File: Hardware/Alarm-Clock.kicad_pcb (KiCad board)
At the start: 2 copper layers, 100 x 61.6 mm, 26 parts, among them IC1 MEGA8-AI, Q1 16Mhz, X1 MINI-USB-32005-201

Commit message: update schematic and board
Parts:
- removed JP11: PINHD-1X4, Alarm-Clock:1X04
- Q1: moved to B.Cu
- turned Q1 to 270 degrees
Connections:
- net Net-(IC1-Pad2) renamed /PD4
- net Net-(IC1-Pad23) renamed /PC0
- net Net-(IC1-Pad24) renamed /PC1
- net Net-(IC1-Pad25) renamed /PC2
- net Net-(IC1-Pad26) renamed /PC3
- net Net-(IC1-Pad27) renamed /PC4
- net Net-(IC1-Pad28) renamed /PC5
- net Net-(IC1-Pad30) renamed /PD0
- net Net-(IC1-Pad31) renamed /PD1
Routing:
- net Net-(JP2-Pad5): track 116.4 -> 123.1 mm, vias 3 -> 2
- net N$59: track 6.67 -> 0.00 mm
- net Net-(C1-Pad2): track 328.2 -> 334.3 mm, vias 12 -> 4
- net N$58: track 6.11 -> 0.00 mm
- net Net-(DIS1-Pad4): track 35.7 -> 34.2 mm, vias 3 -> 2
- net Net-(R2-Pad2): vias 2 -> 0
- net Net-(R1-Pad2): vias 2 -> 0
- net Net-(JP2-Pad4): vias 3 -> 2
- net Net-(JP1-Pad7): vias 1 -> 0
- net Net-(IC1-Pad1): vias 1 -> 0
- net Net-(DIS1-Pad6): vias 3 -> 2
- net Net-(DIS1-Pad3): vias 1 -> 0
- net Net-(DIS1-Pad15): vias 2 -> 0
- net Net-(DIS1-Pad14): vias 1 -> 0
- net Net-(DIS1-Pad13): vias 1 -> 0
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
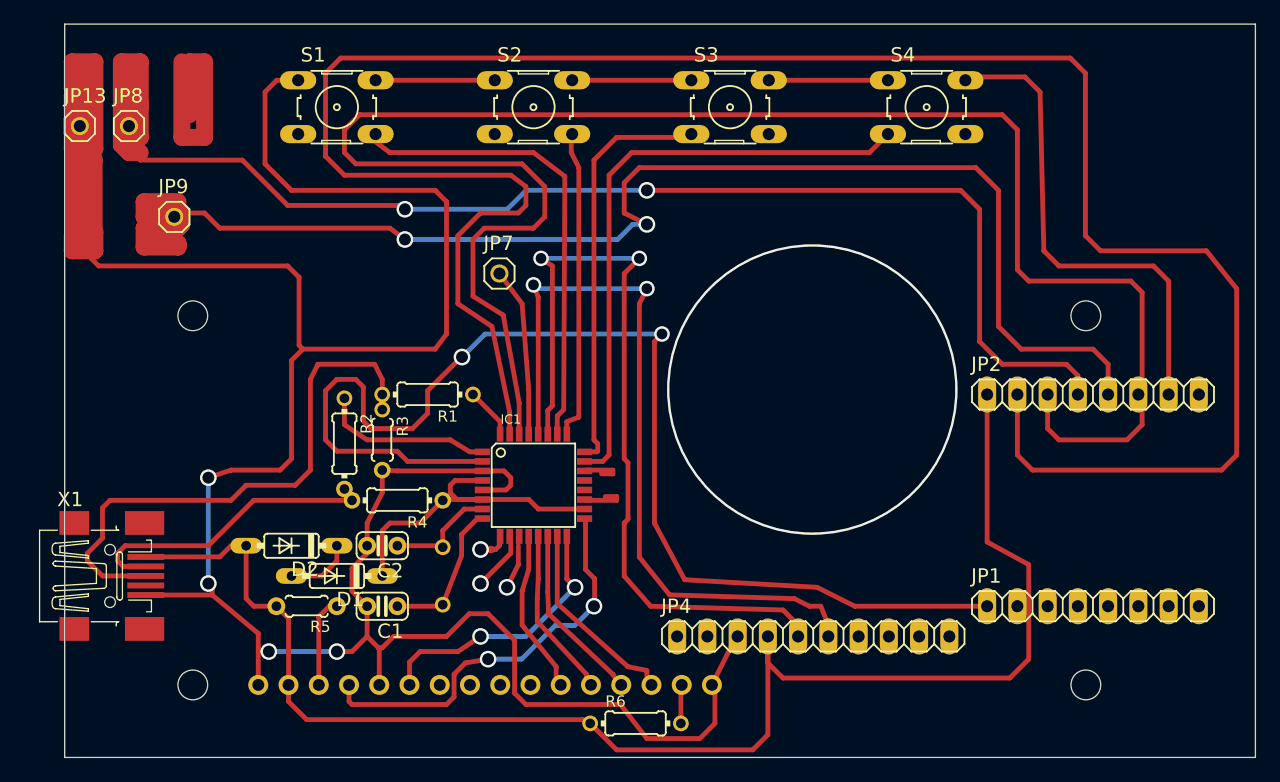
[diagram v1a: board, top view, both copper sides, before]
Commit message: Added 3d models to board
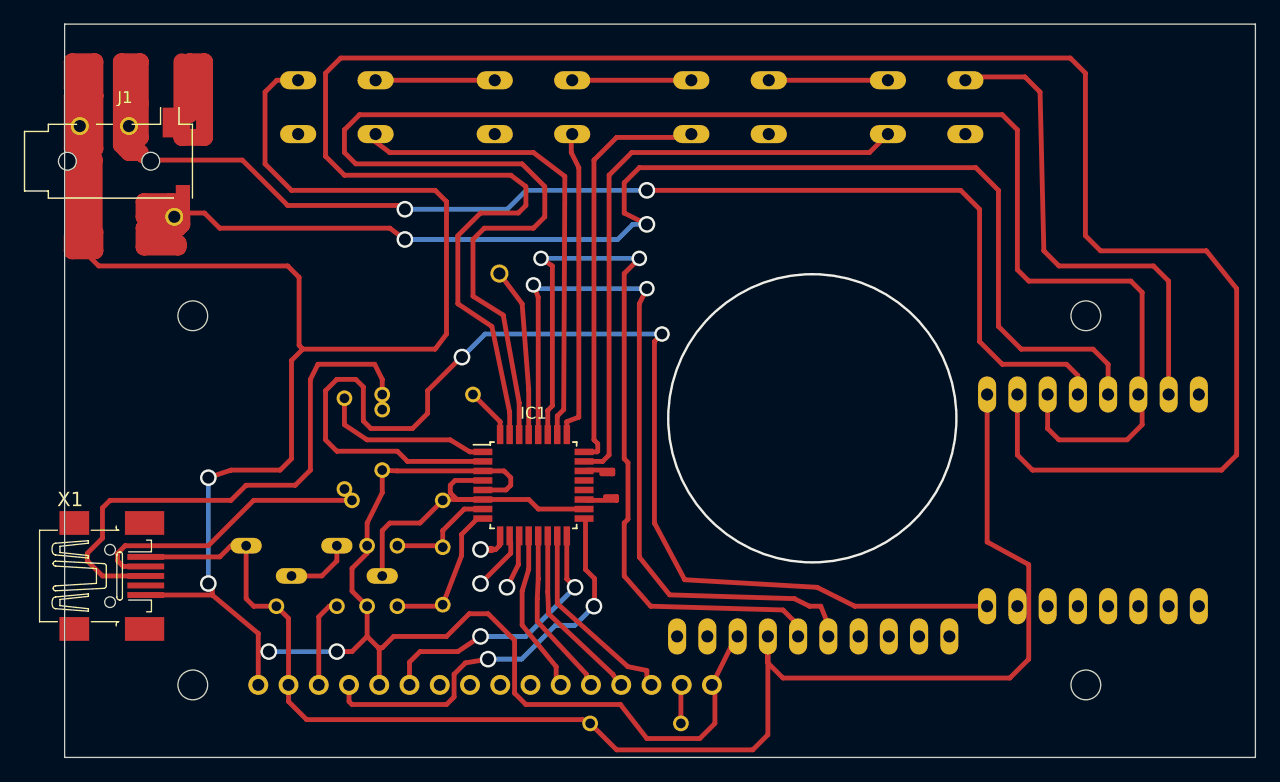
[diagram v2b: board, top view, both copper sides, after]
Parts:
- added J1: AudioJack3, Alarm-Clock:Jack_3.5mm_PJ320D_Horizontal, F.Cu at (103.5, 85.7)
- C1, C2, JP1, JP2, R1, R2, R3, R4, R5, R6, S1, S2, S3, S4: moved to B.Cu
- D1, D2: value 1N4148DO35-7 -> 1N4148; moved to B.Cu
- IC1: footprint Alarm-Clock:TQFP32-08 -> Package_QFP:TQFP-32_7x7mm_P0.8mm
- JP13, JP7, JP8, JP9: value PINHD-1X1 -> PIN; moved to B.Cu
- JP4: value PINHD-1X10 -> RTC; moved to B.Cu
- turned R5 to 0 degrees
- turned S1 to 180 degrees
- turned S2 to 180 degrees
- turned S3 to 180 degrees
- turned S4 to 180 degrees
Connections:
- net Net-(D1-PadC) renamed /VUSB
- net Net-(DIS1-Pad11) renamed /PB0
- net Net-(DIS1-Pad12) renamed /PB1
- net Net-(DIS1-Pad13) renamed /PB2
- net Net-(DIS1-Pad14) renamed /PB3
- net Net-(DIS1-Pad4) renamed /PB5
- net Net-(DIS1-Pad6) renamed /PB4
- net Net-(IC1-Pad1) renamed /PD3
- net Net-(IC1-Pad32) renamed /PD2
- net Net-(JP2-Pad4) renamed /J_R1
- net Net-(JP2-Pad5) renamed /J_S
- C1 pad 2: Net-(C1-Pad2) -> /GND
- C2 pad 2: Net-(C1-Pad2) -> /GND
- D2 pad A: Net-(D2-PadA) -> /VCC
- DIS1 pad 1: Net-(C1-Pad2) -> /GND
- DIS1 pad 16: Net-(C1-Pad2) -> /GND
- DIS1 pad 2: Net-(D2-PadA) -> /VCC
- DIS1 pad 5: Net-(C1-Pad2) -> /GND
- IC1 pad 21: GND -> /GND
- IC1 pad 3: Net-(C1-Pad2) -> /GND
- IC1 pad 5: Net-(C1-Pad2) -> /GND
- JP13 pad 1: Net-(C1-Pad2) -> /GND
- JP2 pad 1: Net-(D2-PadA) -> /VCC
- JP2 pad 7: Net-(C1-Pad2) -> /GND
- JP4 pad 3: Net-(C1-Pad2) -> /GND
- JP4 pad 4: Net-(D2-PadA) -> /VCC
- R3 pad 2: Net-(C1-Pad2) -> /GND
- R5 pad 1: Net-(DIS1-Pad3) -> /VCC
- R5 pad 2: Net-(D2-PadA) -> Net-(DIS1-Pad3)
- R6 pad 1: Net-(D2-PadA) -> /VCC
- S1 pad 1: Net-(C1-Pad2) -> /GND
- S1 pad 2: Net-(C1-Pad2) -> /GND
- S2 pad 1: Net-(C1-Pad2) -> /GND
- S2 pad 2: Net-(C1-Pad2) -> /GND
- S3 pad 1: Net-(C1-Pad2) -> /GND
- S3 pad 2: Net-(C1-Pad2) -> /GND
- S4 pad 1: Net-(C1-Pad2) -> /GND
- S4 pad 2: Net-(C1-Pad2) -> /GND
- X1 pad 1: Net-(D2-PadA) -> /VCC
- X1 pad 5: Net-(C1-Pad2) -> /GND
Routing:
- net Net-(C1-Pad2): track 334.3 -> 0.00 mm, vias 4 -> 0
- net /GND: track 0.00 -> 334.3 mm, vias 0 -> 4
- net Net-(D2-PadA): track 124.8 -> 0.00 mm
- net /VCC: track 0.00 -> 124.8 mm
- net N$57: track 20.3 -> 0.00 mm
- net (no net): track 0.00 -> 20.3 mm
- net /J_R1: track 123.1 -> 121.1 mm
